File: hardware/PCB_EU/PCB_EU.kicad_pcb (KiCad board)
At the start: 4 copper layers, 100 x 100 mm, 200 parts, among them J101 24 V IN, J201 UART 3V3, J301 MEM2061 SPI, J401 SHT 3V3 / GND, J402 SHT SDA / SCL, J403 FLOAT / GND, J411 FAN1: GND / +12, J412 FAN1: TACH / PWM, J421 FAN2: GND / +12, J422 FAN2: TACH / PWM, J501 LED1 + / GND, J601 LED2 + / GND, J602 BAR2 + / GND, J701 PTC + / RETURN, J702 PUMP + / RETURN, Q411 FAN1 AO3422, Q421 FAN2 AO3422, Q501 IRF540ZPBF, Q601 IRF540ZPBF, Q701 BC847B-DIO, Q702 BC857B, Q703 IRF1010ESPBF, Q704 AO3422, SW201 RESET, SW202 BOOT, U101 L7987 3A, U201 AP63203WU-7, U202 ESP32-WROOM-32E-N4, U301 MCP7940N-I/SN, U401 USBLC6-2SC6, U402 USBLC6-2SC6, U501 LM3429MH/NOPB, U601 LM3429MH/NOPB, U801 TC4427AEPA, U802 LM2903D-ST, Y301 32.768k CL7p

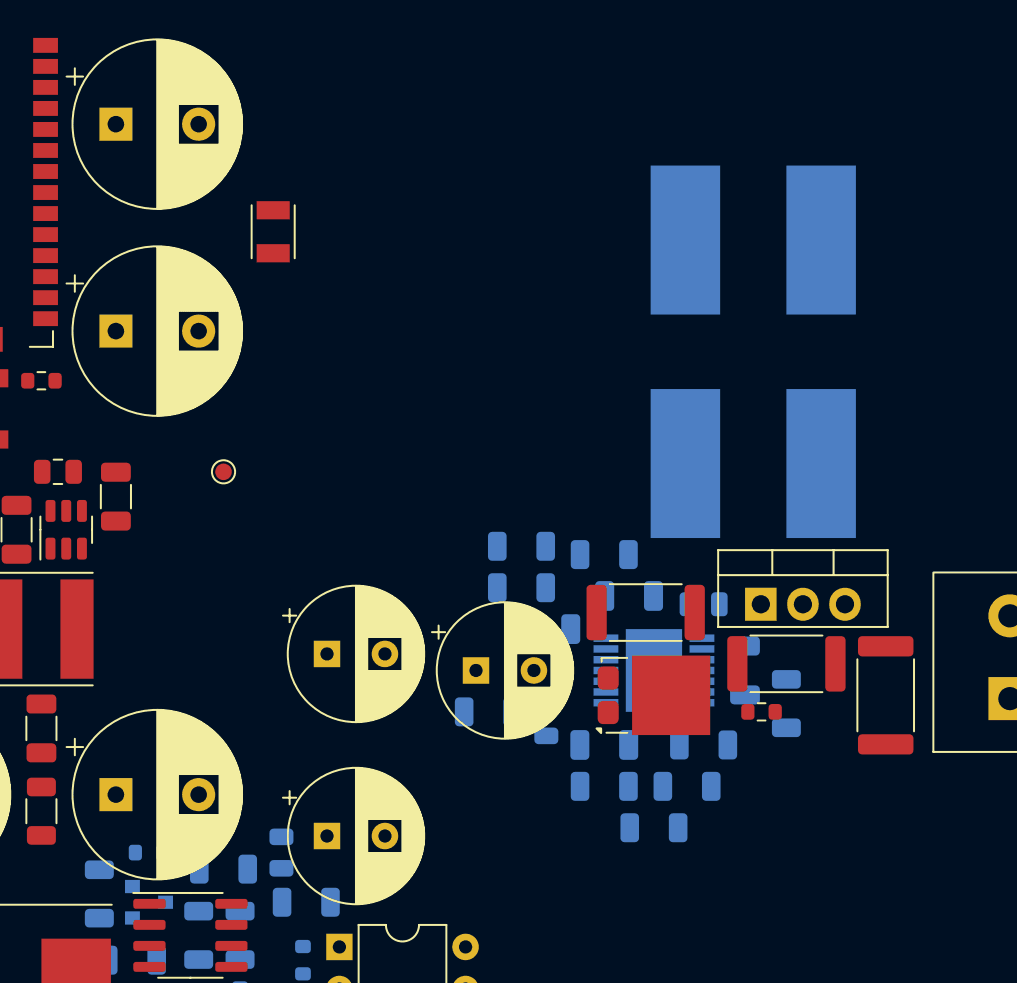
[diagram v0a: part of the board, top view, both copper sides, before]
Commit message: Route initial EU LED1 power connections and add native copper checks
Improve LED1 placement without changing the electrical BOM. Add 40 track segments, 8 vias and an In1 GND plane; verify eight physical copper groups. Keep 361 remaining connections and all mechanical, ampacity and firmware limitations explicit.
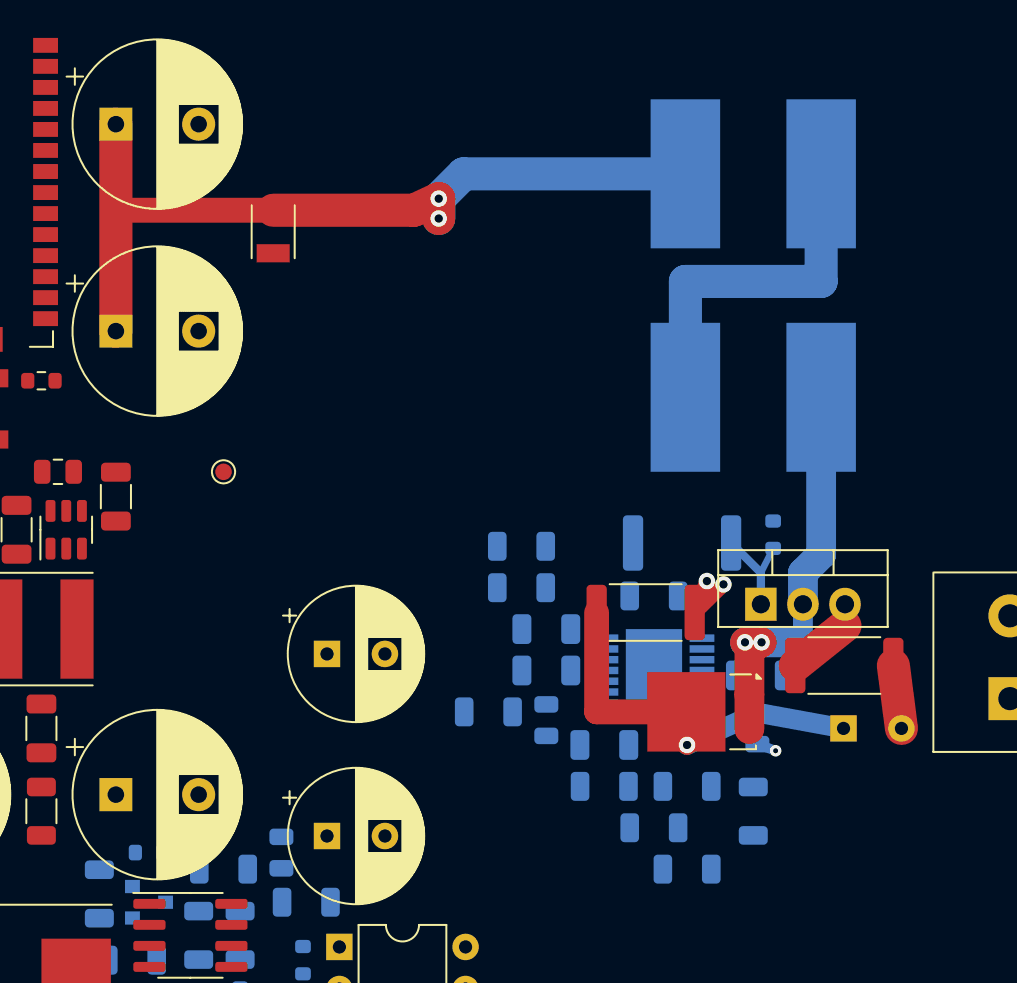
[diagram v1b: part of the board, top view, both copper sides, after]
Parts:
- C508, R803, R804: moved to B.Cu
- moved C508 22.5 mm to (85.5, 50.0)
- moved R504 11.7 mm to (76.0, 58.5), turned to 0 degrees
- moved R804 10.7 mm to (81.2, 38.3), turned to 90 degrees
- moved R803 9.64 mm to (75.7, 38.8), turned to 0 degrees
- moved C511 8.17 mm to (80.2, 50.0), turned to -90 degrees
- moved C507 6.73 mm to (67.5, 46.5)
- moved R503 5.00 mm to (80.0, 55.0), turned to 90 degrees
- moved L501 4.00 mm to (80.0, 16.5)
- moved L502 4.00 mm to (80.0, 30.0)
- moved R507 3.91 mm to (74.0, 42.0)
- moved D501 3.16 mm to (77.0, 49.0), turned to -90 degrees
- moved R501 3.08 mm to (85.5, 46.2), turned to 0 degrees
- moved C504 0.95 mm to (80.4, 46.8), turned to 0 degrees
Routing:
- net +24V_LED1: track 0.00 -> 50.1 mm, vias 0 -> 2
- net LED1_LED_POS: track 0.00 -> 29.8 mm, vias 0 -> 2
- net LED1_SW: track 0.00 -> 25.4 mm, vias 0 -> 2
- net LED1_OUT: track 0.00 -> 23.4 mm, vias 0 -> 1
- net LED1_L_MID: track 0.00 -> 21.7 mm
- net LED1_GATE: track 0.00 -> 6.09 mm
- net LED1_IS: track 0.00 -> 5.14 mm
- net GND: track 0.00 -> 5.00 mm, vias 0 -> 1
- added copper zone on In1.Cu, net GND
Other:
- board text added: "EU-0.1 / PARTIAL LED1 ROUTING / 100 x 100 mm / 4 Cu"
- board text removed: "EU-0.1 / UNROUTED PLACEMENT / 100 x 100 mm / 4 Cu"
